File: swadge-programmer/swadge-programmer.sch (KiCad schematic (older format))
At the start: 26 parts, among them J1 USB_B_Micro, J2 Conn_02x15_Top_Bottom, J3 Conn_02x15_Top_Bottom, J4 ftdi-header, J5 Conn_01x03_Male, SW1 4-1437565-2, SW2 4-1437565-2, SW3 4-1437565-2, SW4 SW_DPDT_x2, SW5 SW_DPDT_x2, U1 BUS_PCIexpress, U2 CP2102N-A01-GQFN24

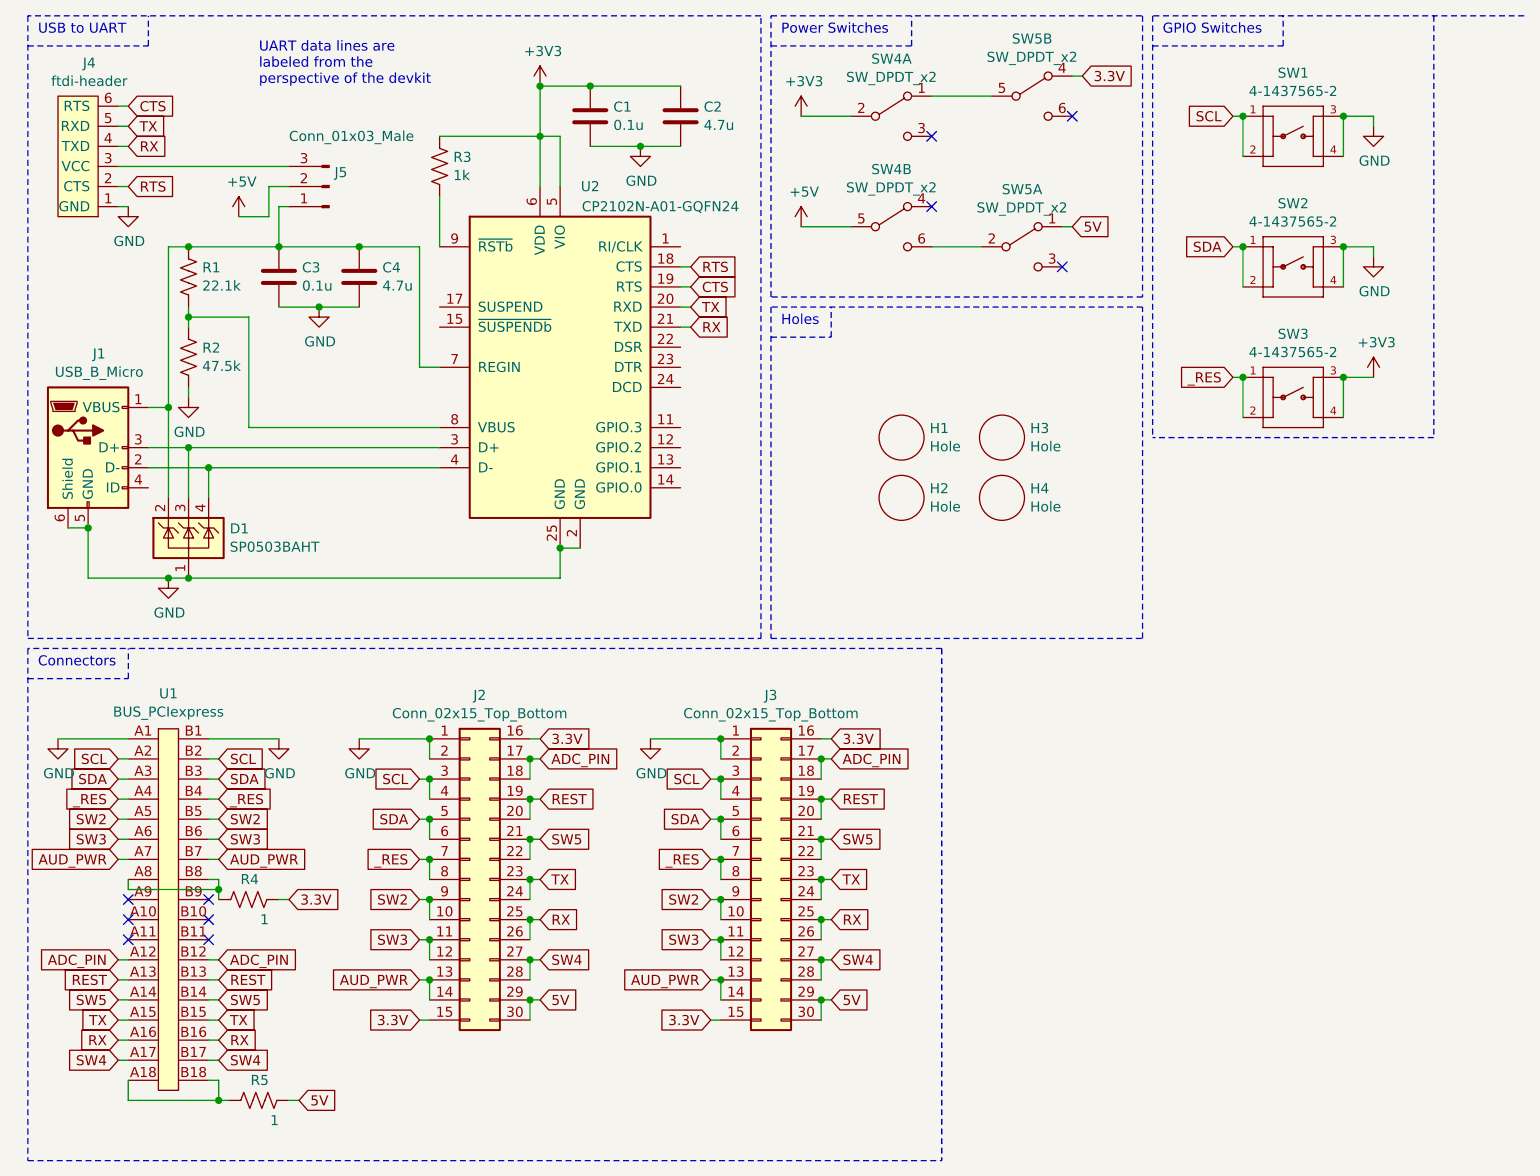
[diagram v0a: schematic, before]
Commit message: Added pin for LED OUT
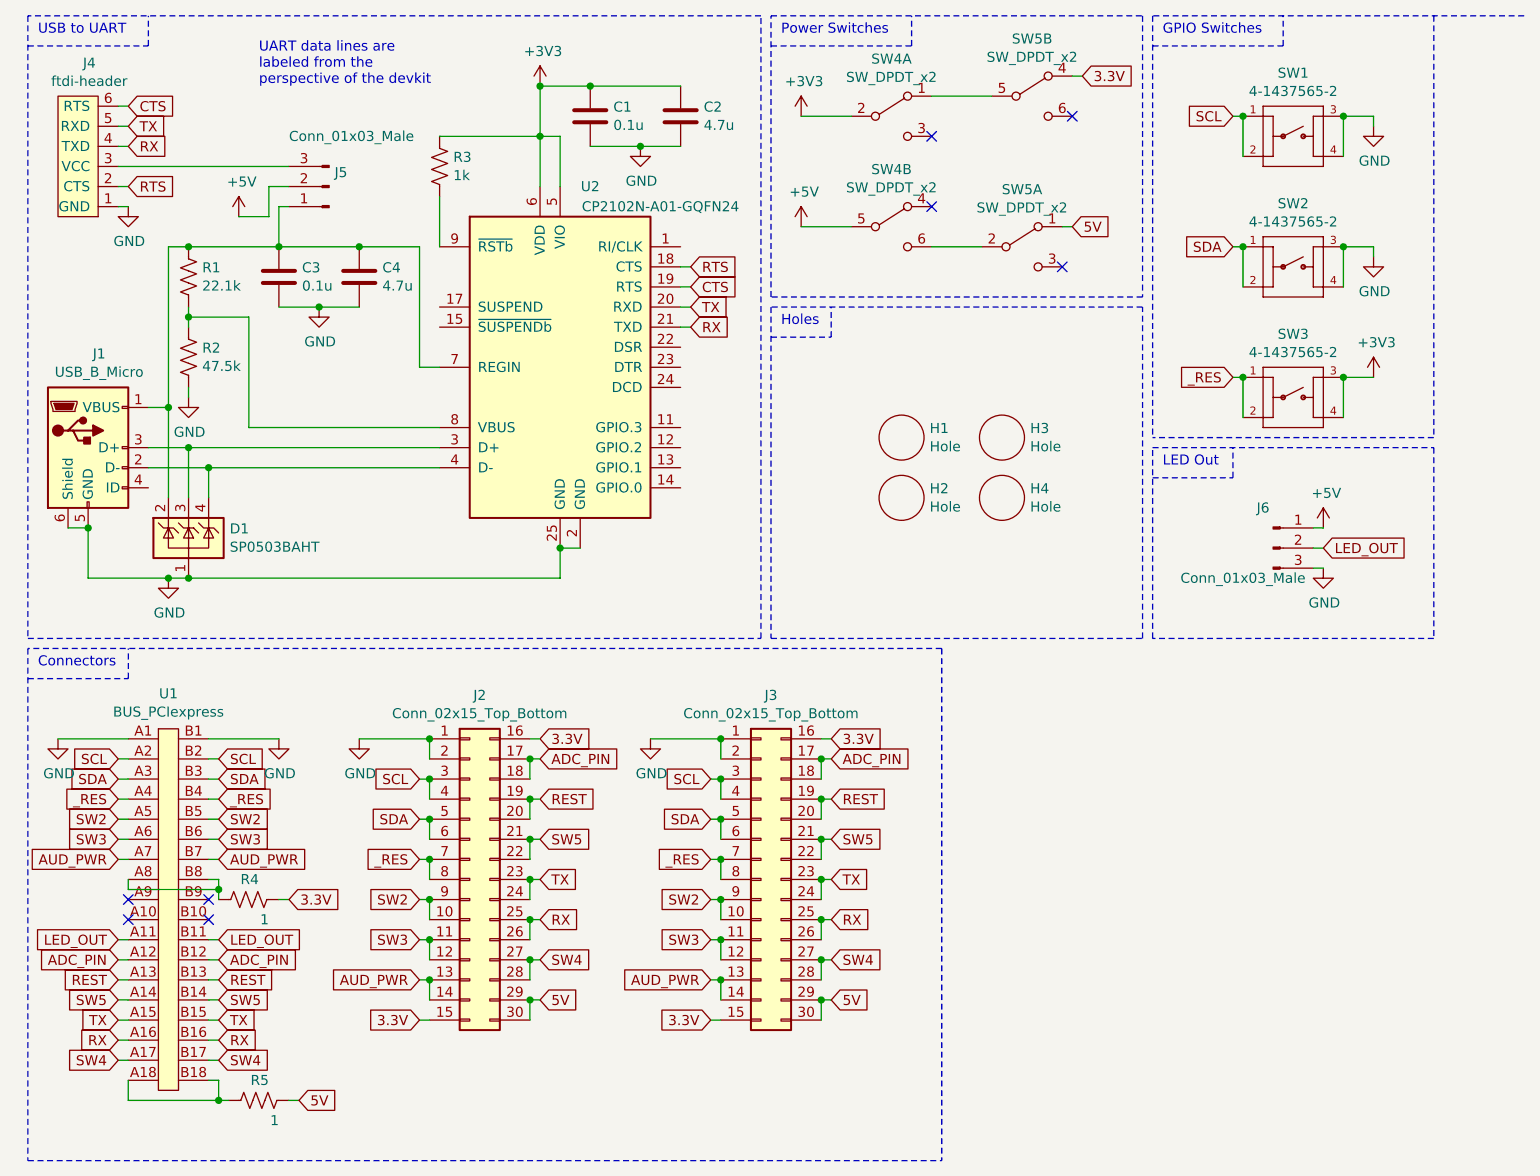
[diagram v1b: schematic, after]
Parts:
- added J6: Conn_01x03_Male, Swadge_Parts:PinHeader_1x03_P2.54mm_Vertical, symbol Swadge_Parts:Conn_01x03_Male
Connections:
- net +5V: now also J6.1 (Pin_1)
- net GND: now also J6.3 (Pin_3)
- net LED_OUT: now reaches U1.A11
- net LED_OUT: now also U1.B11, J6.2 (Pin_2)
- no-connect marks 10 -> 8
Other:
- note added: "LED Out"
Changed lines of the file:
@@
 EESchema Schematic File Version 4
-EELAYER 29 0
+EELAYER 30 0
 EELAYER END
 $Descr A4 11693 8268
@@
 NoConn ~ 1400 4900
 NoConn ~ 1400 5000
-NoConn ~ 1400 5100
-NoConn ~ 1000 5100
 NoConn ~ 1000 5000
 NoConn ~ 1000 4900
@@
 Text GLabel 6500 2300 0    50   Input ~ 0
 _RES
+Text GLabel 950  5100 0    50   Input ~ 0
+LED_OUT
+Text GLabel 1450 5100 2    50   Input ~ 0
+LED_OUT
+Wire Wire Line
+	1400 5100 1450 5100
+Wire Wire Line
+	1000 5100 950  5100
+$Comp
+L Swadge_Parts:Conn_01x03_Male J6
+U 1 1 611EE9D3
+P 6700 3150
+F 0 "J6" H 6650 3350 50  0000 C CNN
+F 1 "Conn_01x03_Male" H 6550 3000 50  0000 C CNN
+F 2 "Swadge_Parts:PinHeader_1x03_P2.54mm_Vertical" H 6600 3250 50  0001 C CNN
+F 3 "~" H 6700 3350 50  0001 C CNN
+F 4 "1849-1003-ND" H 6800 3450 50  0001 C CNN "Digikey"
+F 5 "10" H 6900 3550 50  0001 C CNN "Cost100"
+F 6 "Y" H 7000 3650 50  0001 C CNN "Substitutable"
+	1    6700 3150
+	1    0    0    -1
+$EndComp
+Text GLabel 6950 3150 2    50   Input ~ 0
+LED_OUT
+$Comp
+L Swadge_Parts:GND #PWR015
+U 1 1 611F0346
+P 6950 3250
+F 0 "#PWR015" H 6950 3000 50  0001 C CNN
+F 1 "GND" H 6955 3077 50  0000 C CNN
+F 2 "" H 6950 3250 50  0001 C CNN
+F 3 "" H 6950 3250 50  0001 C CNN
+	1    6950 3250
+	1    0    0    -1
+$EndComp
+$Comp
+L Swadge_Parts:+5V #PWR014
+U 1 1 611F0C47
+P 6950 3050
+F 0 "#PWR014" H 6950 2900 50  0001 C CNN
+F 1 "+5V" H 6965 3223 50  0000 C CNN
+F 2 "" H 6950 3050 50  0001 C CNN
+F 3 "" H 6950 3050 50  0001 C CNN
+	1    6950 3050
+	1    0    0    -1
+$EndComp
+Wire Wire Line
+	6900 3050 6950 3050
+Wire Wire Line
+	6900 3150 6950 3150
+Wire Wire Line
+	6900 3250 6950 3250
+Wire Notes Line
+	6100 2650 7500 2650
+Wire Notes Line
+	7500 2650 7500 3600
+Wire Notes Line
+	7500 3600 6100 3600
+Wire Notes Line
+	6100 3600 6100 2650
+Text Notes 6150 2750 0    50   ~ 0
+LED Out
+Wire Notes Line
+	6100 2800 6500 2800
+Wire Notes Line
+	6500 2800 6500 2650
 $EndSCHEMATC

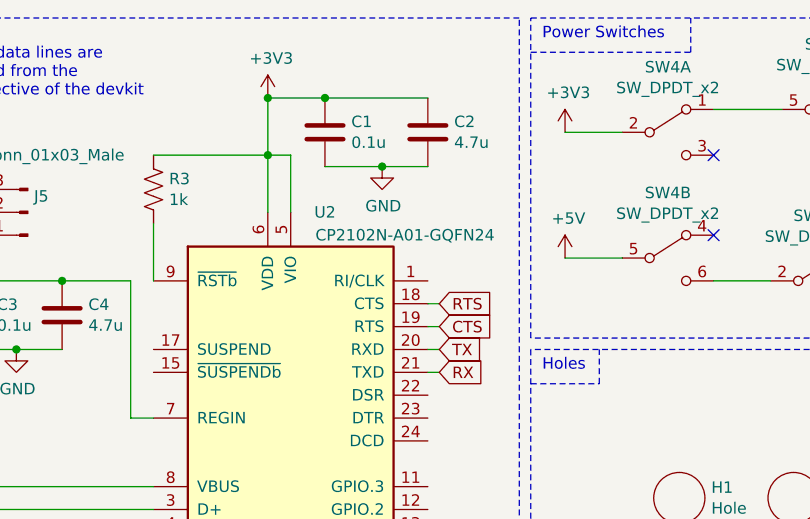
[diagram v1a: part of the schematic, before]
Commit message: Updated CP2012n revision
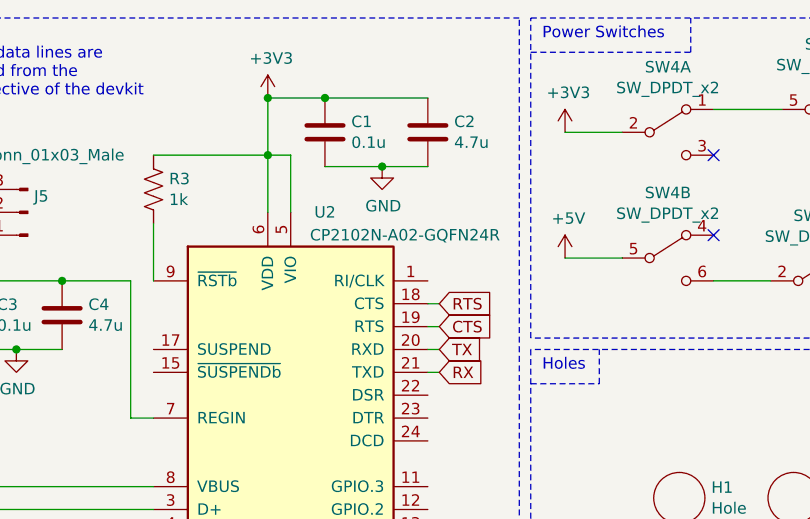
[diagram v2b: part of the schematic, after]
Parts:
- U2: value CP2102N-A01-GQFN24 -> CP2102N-A02-GQFN24R; Digikey 336-4737-1-ND -> 336-5888-1-ND
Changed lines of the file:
@@
 P 3150 2250
 F 0 "U2" H 3300 3150 50  0000 C CNN
-F 1 "CP2102N-A01-GQFN24" H 3650 3050 50  0000 C CNN
+F 1 "CP2102N-A02-GQFN24R" H 3650 3050 50  0000 C CNN
 F 2 "Swadge_Parts:QFN-24-1EP_4x4mm_P0.5mm_EP2.6x2.6mm" H 3600 1450 50  0001 L CNN
 F 3 "http://www.silabs.com/support%20documents/technicaldocs/cp2102n-datasheet.pdf" H 3200 1200 50  0001 C CNN
 F 4 "135" H 0   0   50  0001 C CNN "Cost100"
-F 5 "336-4737-1-ND" H 0   0   50  0001 C CNN "Digikey"
+F 5 "336-5888-1-ND" H 0   0   50  0001 C CNN "Digikey"
 F 6 "Y" H 0   0   50  0001 C CNN "Substitutable"
 	1    3150 2250
